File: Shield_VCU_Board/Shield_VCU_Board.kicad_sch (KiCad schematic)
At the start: 160 parts, among them J1 Conn_02x08_Odd_Even, J10 Main_Supply, J11 Conn_01x40_Socket, J12 TFT Wire, J13 Conn_Molex_TouchPanel, J14 CAN_OUT, J15 Conn_01x04_Socket, J2 Conn_02x10_Odd_Even, J3/1 NXP3, J4 Conn_02x08_Odd_Even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

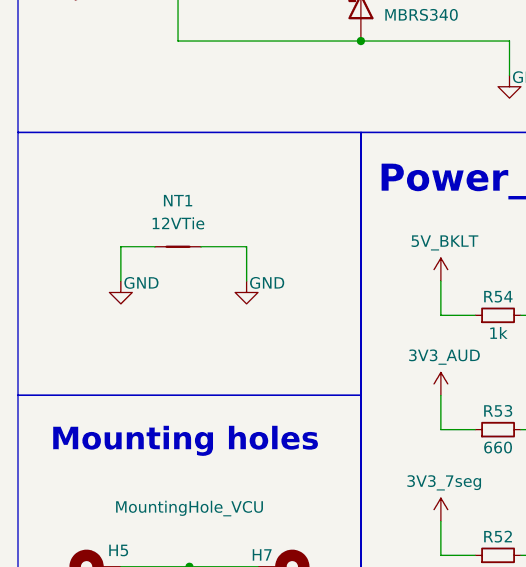
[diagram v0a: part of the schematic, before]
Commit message: SHOTTKY x2 size change
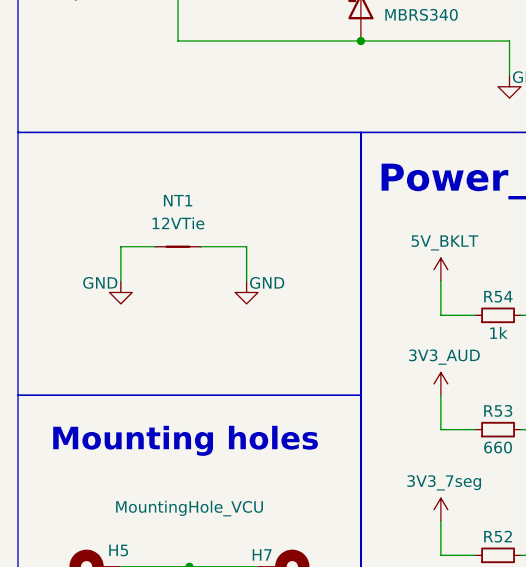
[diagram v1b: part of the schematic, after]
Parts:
- D15, D16: footprint Diode_SMD:D_SMC -> Diode_SMD:D_SMB
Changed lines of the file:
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@@
 		)
 	)
-	(netclass_flag ""
-		(length 2.54)
-		(shape round)
-		(at 59.69 241.3 0)
-		(effects
-			(font
-				(size 1.27 1.27)
-				(color 255 111 53 1)
-			)
-			(justify left bottom)
-		)
-		(property "Netclass" "12V"
-			(at 57.912 237.236 0)
-			(effects
-				(font
-					(size 1.27 1.27)
-				)
-				(justify left)
-			)
-		)
-		(property "Component Class" ""
-			(at -36.83 3.81 0)
-			(effects
-				(font
-					(size 1.27 1.27)
-					(italic yes)
-				)
-			)
-		)
-	)
-	(netclass_flag ""
-		(length 2.54)
-		(shape round)
-		(at 198.12 254 180)
-		(effects
-			(font
-				(size 1.27 1.27)
-				(color 255 106 245 1)
-			)
-			(justify right bottom)
-		)
-		(property "Netclass" "PowerV"
-			(at 198.12 258.064 0)
-			(effects
-				(font
-					(size 1.27 1.27)
-				)
-				(justify right)
-			)
-		)
-		(property "Component Class" ""
-			(at 318.77 -31.75 0)
-			(effects
-				(font
-					(size 1.27 1.27)
-					(italic yes)
-				)
-				(justify left)
-			)
-		)
-	)
-	(netclass_flag ""
-		(length 2.54)
-		(shape round)
-		(at 199.39 292.1 180)
-		(effects
-			(font
-				(size 1.27 1.27)
-				(color 255 106 245 1)
-			)
-			(justify right bottom)
-		)
-		(property "Netclass" "PowerV"
-			(at 199.644 296.164 0)
-			(effects
-				(font
-					(size 1.27 1.27)
-				)
-				(justify left)
-			)
-		)
-		(property "Component Class" ""
-			(at 78.74 6.35 0)
-			(effects
-				(font
-					(size 1.27 1.27)
-					(italic yes)
-				)
-			)
-		)
-	)
-	(netclass_flag ""
-		(length 2.54)
-		(shape round)
-		(at 200.66 335.28 180)
-		(effects
-			(font
-				(size 1.27 1.27)
-				(color 255 106 245 1)
-			)
-			(justify right bottom)
-		)
-		(property "Netclass" "PowerV"
-			(at 200.66 339.598 0)
-			(effects
-				(font
-					(size 1.27 1.27)
-				)
-				(justify left)
-			)
-		)
-		(property "Component Class" ""
-			(at 80.01 49.53 0)
-			(effects
-				(font
-					(size 1.27 1.27)
-					(italic yes)
-				)
-			)
-		)
-	)
-	(netclass_flag ""
-		(length 2.54)
-		(shape round)
-		(at 199.39 381 180)
-		(effects
-			(font
-				(size 1.27 1.27)
-				(color 255 106 245 1)
-			)
-			(justify right bottom)
-		)
-		(property "Netclass" "PowerV"
-			(at 199.644 385.064 0)
-			(effects
-				(font
-					(size 1.27 1.27)
-				)
-				(justify left)
-			)
-		)
-		(property "Component Class" ""
-			(at 78.74 95.25 0)
-			(effects
-				(font
-					(size 1.27 1.27)
-					(italic yes)
-				)
-			)
-		)
-	)
 	(symbol
 		(lib_id "Interface_Expansion:AS1115-BSST")
@@
 			)
 		)
-		(property "Footprint" "Diode_SMD:D_SMC"
+		(property "Footprint" "Diode_SMD:D_SMB"
 			(at 306.07 254.254 0)
 			(effects
@@
 			)
 		)
-		(property "Footprint" "Diode_SMD:D_SMC"
+		(property "Footprint" "Diode_SMD:D_SMB"
 			(at 42.164 245.11 0)
 			(effects
@@
 		)
 		(property "Value" "GND"
-			(at 26.416 275.844 0)
+			(at 21.844 275.844 0)
 			(effects
 				(font

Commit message: Logos_Added
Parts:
- D1, D2, D3, D4: footprint ALibrary:LED_Cree-PLCC4_3.2x2.8mm_CCW_Corrected -> ALibrary:LED_Cree-PLCC4_3.2x2.8mm_CCW_Orange
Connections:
- net LED1_PTB9 renamed LED1_PTD26
- net LED2_PTA12 renamed LED2_PTD29
- net LED3_PTA24 renamed LED3_PTD28
- net LED4_PTA25 renamed LED4_PTD31
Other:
- note added: "[Orange LED]"
- moved on the sheet: C10, C11, C35, C38, C39, C43, C44, C8, C9, D16, D17, FB1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

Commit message: Gerber_files_created_V1.0
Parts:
- U10: value TPS61165DBV -> TPS61165-Q1
- U7: value FT812 -> FT813Q
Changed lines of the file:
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@@
 	)
 	(junction
-		(at 270.51 260.35)
-		(diameter 0)
-		(color 0 0 0 0)
-	)
-	(junction
 		(at 50.8 248.92)
 		(diameter 0)
@@
 	)
 	(junction
+		(at 270.51 260.35)
+		(diameter 0)
+		(color 0 0 0 0)
+	)
+	(junction
 		(at 180.34 344.17)
 		(diameter 0)
@@
 	(wire
 		(pts
+			(xy 270.51 260.35) (xy 275.59 260.35)
+		)
+		(stroke
+			(width 0)
+			(type default)
+		)
+	)
+	(wire
+		(pts
 			(xy 486.41 118.11) (xy 488.95 118.11)
 		)
@@
 	(wire
 		(pts
-			(xy 270.51 260.35) (xy 275.59 260.35)
-		)
-		(stroke
-			(width 0)
-			(type default)
-		)
-	)
-	(wire
-		(pts
 			(xy 527.05 337.82) (xy 527.05 360.68)
 		)
@@
 			)
 		)
-		(property "Value" "FT812"
+		(property "Value" "FT813Q"
 			(at 402.082 94.234 0)
 			(effects
@@
 			)
 		)
-		(property "Value" "TPS61165DBV"
+		(property "Value" "TPS61165-Q1"
 			(at 291.084 274.574 0)
 			(effects

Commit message: NXP_correction for3D_Enclosure
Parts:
- D1, D2, D3, D4: value LED -> AA35*
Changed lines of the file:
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@@
 			)
 		)
-		(property "Value" "LED"
-			(at 36.83 346.202 0)
+		(property "Value" "AA35*"
+			(at 37.338 353.06 0)
 			(effects
 				(font
@@
 			)
 		)
-		(property "Value" "LED"
-			(at 38.354 361.188 0)
+		(property "Value" "AA35*"
+			(at 38.354 368.3 0)
 			(effects
 				(font
@@
 			)
 		)
-		(property "Value" "LED"
-			(at 36.83 376.682 0)
+		(property "Value" "AA35*"
+			(at 37.592 383.286 0)
 			(effects
 				(font
@@
 			)
 		)
-		(property "Value" "LED"
-			(at 36.83 390.144 0)
+		(property "Value" "AA35*"
+			(at 37.338 397.51 0)
 			(effects
 				(font

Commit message: Revision_added
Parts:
- D15, D16: value MBRS340 -> SS34
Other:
- company: EVR TOVOR IASI -> EVR IASI
- title: VCU DASHBOARD V2.0 -> VCU DASHBOARD V1.0
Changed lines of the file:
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@@
 	(paper "A2")
 	(title_block
-		(title "VCU DASHBOARD V2.0")
+		(title "VCU DASHBOARD V1.0")
 		(date "2026-03-20")
-		(company "EVR TOVOR IASI")
+		(rev "Viorel Stoica")
+		(company "EVR IASI")
 	)
 	(rectangle
@@
 			)
 		)
-		(property "Value" "MBRS340"
+		(property "Value" "SS34"
 			(at 306.3875 247.65 0)
 			(effects
@@
 			)
 		)
-		(property "Value" "MBRS340"
+		(property "Value" "SS34"
 			(at 53.34 246.0624 90)
 			(effects

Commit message: MountingHoles:change to M3
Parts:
- H5, H6, H7, H8: footprint MountingHole:MountingHole_2.7mm_M2.5_Pad -> MountingHole:MountingHole_3.2mm_M3_DIN965_Pad
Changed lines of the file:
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@@
 			)
 		)
-		(property "Footprint" "MountingHole:MountingHole_2.7mm_M2.5_Pad"
+		(property "Footprint" "MountingHole:MountingHole_3.2mm_M3_DIN965_Pad"
 			(at 41.91 314.96 0)
 			(effects
@@
 			)
 		)
-		(property "Footprint" "MountingHole:MountingHole_2.7mm_M2.5_Pad"
+		(property "Footprint" "MountingHole:MountingHole_3.2mm_M3_DIN965_Pad"
 			(at 21.59 314.96 0)
 			(effects
@@
 			)
 		)
-		(property "Footprint" "MountingHole:MountingHole_2.7mm_M2.5_Pad"
+		(property "Footprint" "MountingHole:MountingHole_3.2mm_M3_DIN965_Pad"
 			(at 41.91 307.34 0)
 			(effects
@@
 			)
 		)
-		(property "Footprint" "MountingHole:MountingHole_2.7mm_M2.5_Pad"
+		(property "Footprint" "MountingHole:MountingHole_3.2mm_M3_DIN965_Pad"
 			(at 21.59 307.34 0)
 			(effects

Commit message: PartList_added
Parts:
- D15, D16: value SS34 -> SSC54*
- R22, R52, R53: value 660 -> 220
- R27: footprint Resistor_SMD:R_0201_0603Metric_Pad0.64x0.40mm_HandSolder -> Resistor_SMD:R_0603_1608Metric_Pad0.98x0.95mm_HandSolder
- R54: value 1k -> 660
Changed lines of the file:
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@@
 			)
 		)
-		(property "Value" "660"
+		(property "Value" "220"
 			(at 66.04 294.132 90)
 			(effects
@@
 			)
 		)
-		(property "Value" "SS34"
+		(property "Value" "SSC54*"
 			(at 306.3875 247.65 0)
 			(effects
@@
 			)
 		)
-		(property "Footprint" "Resistor_SMD:R_0201_0603Metric_Pad0.64x0.40mm_HandSolder"
+		(property "Footprint" "Resistor_SMD:R_0603_1608Metric_Pad0.98x0.95mm_HandSolder"
 			(at 481.33 143.51 0)
 			(effects
@@
 			)
 		)
-		(property "Value" "660"
+		(property "Value" "220"
 			(at 66.04 308.102 90)
 			(effects
@@
 			)
 		)
-		(property "Value" "660"
+		(property "Value" "220"
 			(at 66.04 320.802 90)
 			(effects
@@
 			)
 		)
-		(property "Value" "1k"
+		(property "Value" "660"
 			(at 66.04 281.432 90)
 			(effects
@@
 			)
 		)
-		(property "Value" "SS34"
+		(property "Value" "SSC54*"
 			(at 53.34 246.0624 90)
 			(effects

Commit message: LastBOM added
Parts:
- FB1, FB2: footprint Inductor_SMD:L_Neosid_SM-PIC0512H -> Inductor_SMD:L_1206_3216Metric_Pad1.22x1.90mm_HandSolder
- J15: footprint Connector_PinHeader_2.54mm:PinHeader_1x04_P2.54mm_Vertical_SMD_Pin1Left -> Connector_PinHeader_2.54mm:PinHeader_1x04_P2.54mm_Vertical
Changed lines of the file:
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@@
 			)
 		)
-		(property "Footprint" "Inductor_SMD:L_Neosid_SM-PIC0512H"
+		(property "Footprint" "Inductor_SMD:L_1206_3216Metric_Pad1.22x1.90mm_HandSolder"
 			(at 393.7 371.348 90)
 			(effects
@@
 			)
 		)
-		(property "Footprint" "Inductor_SMD:L_Neosid_SM-PIC0512H"
+		(property "Footprint" "Inductor_SMD:L_1206_3216Metric_Pad1.22x1.90mm_HandSolder"
 			(at 393.7 384.048 90)
 			(effects
@@
 			)
 		)
-		(property "Footprint" "Connector_PinHeader_2.54mm:PinHeader_1x04_P2.54mm_Vertical_SMD_Pin1Left"
+		(property "Footprint" "Connector_PinHeader_2.54mm:PinHeader_1x04_P2.54mm_Vertical"
 			(at 96.52 163.83 0)
 			(effects
